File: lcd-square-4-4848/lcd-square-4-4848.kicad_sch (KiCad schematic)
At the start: 43 parts, among them J1 SWD, J2 Conn_01x40_MountingPin, J3 Micro_SD_Card_Det1, SW1 BOOT0, SW2 RST, U1 siplex-som-s16, U2 TPS61169

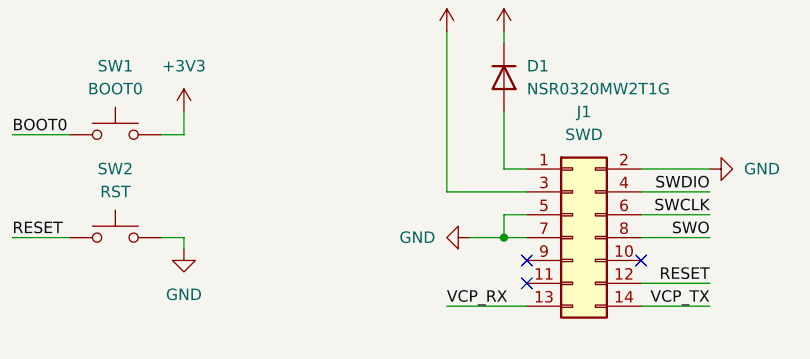
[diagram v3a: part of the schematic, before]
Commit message: LCD 5 inch, Finished SD card, Touch, Buzzer etc, LCD Bar 3.4, Adding resistor on st-link, not finished yet
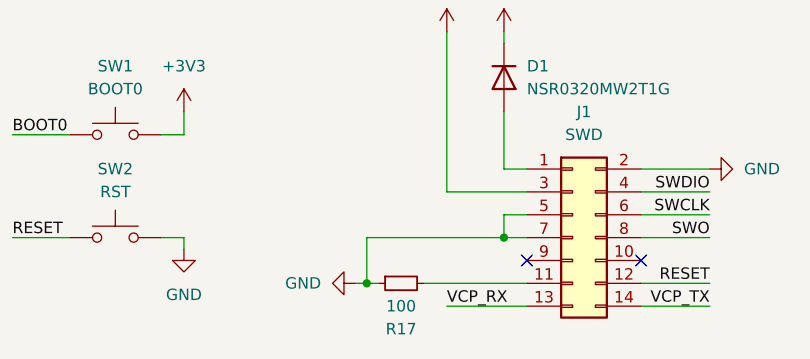
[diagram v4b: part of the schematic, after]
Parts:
- added R17: 100, Resistor_SMD:R_0402_1005Metric, symbol Device:R_Small
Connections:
- net GND: now also R17.1
- net at J1.11 (Pin_11): now also R17.2
- no-connect marks 5 -> 4
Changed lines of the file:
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@@
 	)
 	(junction
+		(at 129.54 189.23)
+		(diameter 0)
+		(color 0 0 0 0)
+	)
+	(junction
 		(at 185.42 66.04)
 		(diameter 0)
@@
 	)
 	(no_connect
-		(at 147.32 189.23)
-	)
-	(no_connect
 		(at 251.46 52.07)
 	)
@@
 	(wire
 		(pts
+			(xy 135.89 189.23) (xy 147.32 189.23)
+		)
+		(stroke
+			(width 0)
+			(type default)
+		)
+	)
+	(wire
+		(pts
 			(xy 24.13 69.85) (xy 36.83 69.85)
 		)
@@
 	(wire
 		(pts
-			(xy 140.97 184.15) (xy 144.78 184.15)
-		)
-		(stroke
-			(width 0)
-			(type default)
-		)
-	)
-	(wire
-		(pts
 			(xy 72.39 52.07) (xy 64.77 52.07)
 		)
@@
 	(wire
 		(pts
+			(xy 129.54 189.23) (xy 130.81 189.23)
+		)
+		(stroke
+			(width 0)
+			(type default)
+		)
+	)
+	(wire
+		(pts
 			(xy 24.13 49.53) (xy 36.83 49.53)
 		)
@@
 	(wire
 		(pts
+			(xy 129.54 184.15) (xy 129.54 189.23)
+		)
+		(stroke
+			(width 0)
+			(type default)
+		)
+	)
+	(wire
+		(pts
 			(xy 24.13 95.25) (xy 36.83 95.25)
 		)
@@
 	(wire
 		(pts
+			(xy 128.27 189.23) (xy 129.54 189.23)
+		)
+		(stroke
+			(width 0)
+			(type default)
+		)
+	)
+	(wire
+		(pts
 			(xy 64.77 39.37) (xy 72.39 39.37)
 		)
@@
 	(wire
 		(pts
+			(xy 129.54 184.15) (xy 144.78 184.15)
+		)
+		(stroke
+			(width 0)
+			(type default)
+		)
+	)
+	(wire
+		(pts
 			(xy 185.42 76.2) (xy 185.42 74.93)
 		)
@@
 	)
 	(symbol
+		(lib_id "power:GND")
+		(at 128.27 189.23 270)
+		(unit 1)
+		(exclude_from_sim no)
+		(in_bom yes)
+		(on_board yes)
+		(dnp no)
+		(fields_autoplaced yes)
+		(property "Reference" "#PWR07"
+			(at 121.92 189.23 0)
+			(effects
+				(font
+					(size 1.27 1.27)
+				)
+				(hide yes)
+			)
+		)
+		(property "Value" "GND"
+			(at 124.46 189.2299 90)
+			(effects
+				(font
+					(size 1.27 1.27)
+				)
+				(justify right)
+			)
+		)
+		(property "Footprint" ""
+			(at 128.27 189.23 0)
+			(effects
+				(font
+					(size 1.27 1.27)
+				)
+				(hide yes)
+			)
+		)
+		(property "Datasheet" ""
+			(at 128.27 189.23 0)
+			(effects
+				(font
+					(size 1.27 1.27)
+				)
+				(hide yes)
+			)
+		)
+		(property "Description" "Power symbol creates a global label with name \"GND\" , ground"
+			(at 128.27 189.23 0)
+			(effects
+				(font
+					(size 1.27 1.27)
+				)
+				(hide yes)
+			)
+		)
+		(pin "1"
+		)
+		(instances
+			(project "lcd-square-4-4848"
+				(path "/a9fe5be7-3a80-455e-a721-d53819db4a52"
+					(reference "#PWR07")
+					(unit 1)
+				)
+			)
+		)
+	)
+	(symbol
 		(lib_id "Device:R_Pack04")
 		(at 95.25 64.77 90)
@@
 	(symbol
 		(lib_id "Device:R_Small")
-		(at 214.63 119.38 0)
-		(mirror y)
+		(at 133.35 189.23 90)
+		(mirror x)
 		(unit 1)
 		(exclude_from_sim no)
@@
 		(on_board yes)
 		(dnp no)
-		(property "Reference" "R5"
-			(at 212.09 118.1099 0)
+		(property "Reference" "R17"
+			(at 133.35 194.31 90)
 			(effects
 				(font
 					(size 1.27 1.27)
 				)
-				(justify left)
 			)
 		)
-		(property "Value" "2K2"
-			(at 212.09 120.6499 0)
+		(property "Value" "100"
+			(at 133.35 191.77 90)
 			(effects
 				(font
 					(size 1.27 1.27)
 				)
-				(justify left)
 			)
 		)
 		(property "Footprint" "Resistor_SMD:R_0402_1005Metric"
-			(at 214.63 119.38 0)
+			(at 133.35 189.23 0)
 			(effects
 				(font
@@
 		)
 		(property "Datasheet" "~"
-			(at 214.63 119.38 0)
+			(at 133.35 189.23 0)
 			(effects
 				(font
@@
 		)
 		(property "Description" "Resistor, small symbol"
-			(at 214.63 119.38 0)
+			(at 133.35 189.23 0)
 			(effects
 				(font
@@
 			)
 		)
-		(pin "2"
-		)
 		(pin "1"
 		)
+		(pin "2"
+		)
 		(instances
 			(project "lcd-square-4-4848"
 				(path "/a9fe5be7-3a80-455e-a721-d53819db4a52"
-					(reference "R5")
+					(reference "R17")
 					(unit 1)
 				)
@@
 	)
 	(symbol
-		(lib_id "power:GND")
-		(at 140.97 184.15 270)
+		(lib_id "Device:R_Small")
+		(at 214.63 119.38 0)
+		(mirror y)
 		(unit 1)
 		(exclude_from_sim no)
@@
 		(on_board yes)
 		(dnp no)
-		(fields_autoplaced yes)
-		(property "Reference" "#PWR010"
-			(at 134.62 184.15 0)
+		(property "Reference" "R5"
+			(at 212.09 118.1099 0)
 			(effects
 				(font
 					(size 1.27 1.27)
 				)
-				(hide yes)
+				(justify left)
 			)
 		)
-		(property "Value" "GND"
-			(at 137.16 184.1499 90)
+		(property "Value" "2K2"
+			(at 212.09 120.6499 0)
 			(effects
 				(font
 					(size 1.27 1.27)
 				)
-				(justify right)
+				(justify left)
 			)
 		)
-		(property "Footprint" ""
-			(at 140.97 184.15 0)
+		(property "Footprint" "Resistor_SMD:R_0402_1005Metric"
+			(at 214.63 119.38 0)
 			(effects
 				(font
@@
 			)
 		)
-		(property "Datasheet" ""
-			(at 140.97 184.15 0)
+		(property "Datasheet" "~"
+			(at 214.63 119.38 0)
 			(effects
 				(font
@@
 			)
 		)
-		(property "Description" "Power symbol creates a global label with name \"GND\" , ground"
-			(at 140.97 184.15 0)
+		(property "Description" "Resistor, small symbol"
+			(at 214.63 119.38 0)
 			(effects
 				(font
@@
 			)
 		)
+		(pin "2"
+		)
 		(pin "1"
 		)
@@
 			(project "lcd-square-4-4848"
 				(path "/a9fe5be7-3a80-455e-a721-d53819db4a52"
-					(reference "#PWR010")
+					(reference "R5")
 					(unit 1)
 				)

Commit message: LCD 5inch, finished tracks, LCD square, Adding MAX98357A
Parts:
- removed U1: siplex-som-s16, siplex:siplex-som-s16, symbol siplex-som:siplex-som-s16
- added C11: 10u, Capacitor_SMD:C_0805_2012Metric, symbol Device:C
- added J5: Conn_01x02_MountingPin, Connector_Hirose:Hirose_DF13C_CL535-0402-2-51_1x02-1MP_P1.25mm_Vertical, symbol Connector_Generic_MountingPin:Conn_01x02_MountingPin
- added R18: 1M, Resistor_SMD:R_0402_1005Metric, symbol Device:R_Small
- added R19: 100K, Resistor_SMD:R_0402_1005Metric, symbol Device:R_Small
- added U1: MAX98357A, Package_DFN_QFN:TQFN-16-1EP_3x3mm_P0.5mm_EP1.23x1.23mm, symbol Audio:MAX98357A
- added U3: siplex-som-s16, siplex:siplex-som-s16, symbol siplex-som:siplex-som-s16
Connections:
- net +3V3: now also U3.42 (3V3_OUT)
- net B0: now also U3.70 (B0)
- net B1: now also U3.71 (B1)
- net B2: now also U3.72 (B2)
- net B3: now also U3.73 (B3)
- net B4: now also U3.74 (B4)
- net B5: now also U3.75 (B5)
- net B6: now also U3.76 (B6)
- net B7: now also U3.77 (B7)
- net BOOT0: now also U3.84 (BOOT0)
- net CLK: now also U3.7 (PC1)
- net CMD: now also U3.9 (PA0)
- net DAT0: now also U3.23 (PB14)
- net DAT1: now also U3.24 (PB15)
- net DAT2: now also U3.39 (PG11)
- net DAT3: now also U3.40 (PB4)
- net G0: now also U3.62 (G0)
- net G1: now also U3.63 (G1)
- net G2: now also U3.64 (G2)
- net G3: now also U3.65 (G3)
- net G4: now also U3.66 (G4)
- net G5: now also U3.67 (G5)
- net G6: now also U3.68 (G6)
- net G7: now also U3.69 (G7)
- net GND: now also C11.2, J5.MP (MountPin), R19.2, U1.11 (GND), U1.15 (GND), U1.17 (PAD), U1.3 (GND), U3.43 (GND), U3.44 (GND), U3.47 (GND), U3.5 (GND), U3.50 (GND), U3.53 (GND), U3.78 (GND), U3.80 (GND), U3.87 (GND)
- net LCD_BLK: now also U3.16 (PB0)
- net LCD_RST: now also U3.14 (PA6)
- net LCD_SPI_CLK: now also U3.15 (PA5)
- net LCD_SPI_CS: now also U3.12 (PA3)
- net LCD_SPI_DAT: now also U3.13 (PA7)
- net LCD_TP_INT: now also U3.1 (PB7)
- net LCD_TP_RST: now also U3.4 (PH4)
- net LCD_TP_SCL: now also U3.2 (PB8)
- net LCD_TP_SDA: now also U3.3 (PB9)
- net LED0: now also U3.22 (PB11)
- net LED1: now also U3.21 (PB13)
- net R0: now also U3.54 (R0)
- net R1: now also U3.55 (R1)
- net R2: now also U3.56 (R2)
- net R3: now also U3.57 (R3)
- net R4: now also U3.58 (R4)
- net R5: now also U3.59 (R5)
- net R6: now also U3.60 (R6)
- net R7: now also U3.61 (R7)
- net RESET: now also U3.85 (RESET)
- net SD_DET: now also U3.25 (PH7)
- net SWCLK: now also U3.46 (SWCLK)
- net SWDIO: now also U3.45 (SWDIO)
- net SWO: now also U3.52 (SWO)
- net USB_DN: now also U3.48 (USB_DN)
- net USB_DP: now also U3.49 (USB_DP)
- net USB_VBUS_DET: now also U3.51 (USB_VBUS_DET)
- net VBAT: now also U3.86 (VBAT)
- net VBUS: now also C11.1, U1.7 (VDD), U1.8 (VDD), U3.41 (VIN)
- net at RN4.5 (R4.2): now also U3.79 (LCD_CLK)
- net at RN4.8 (R1.2): now also U3.83 (LCD_DE)
- net at RN4.7 (R2.2): now also U3.82 (LCD_VSYNC)
- net at RN4.6 (R3.2): now also U3.81 (LCD_HSYNC)
- new net: J5.1 (Pin_1), U1.9 (OUTP)
- new net: J5.2 (Pin_2), U1.10 (OUTN)
- new net: R18.2, U1.4 (~{SD_MODE})
- new net: R19.1, U1.2 (GAIN_SLOT)
- new net I2S_SCLK: U1.16 (BCLK)
- new net I2S_SDO: U1.1 (DIN)
- new net I2S_WS: U1.14 (LRCLK)
- new net ~{SD_MODE}: R18.1

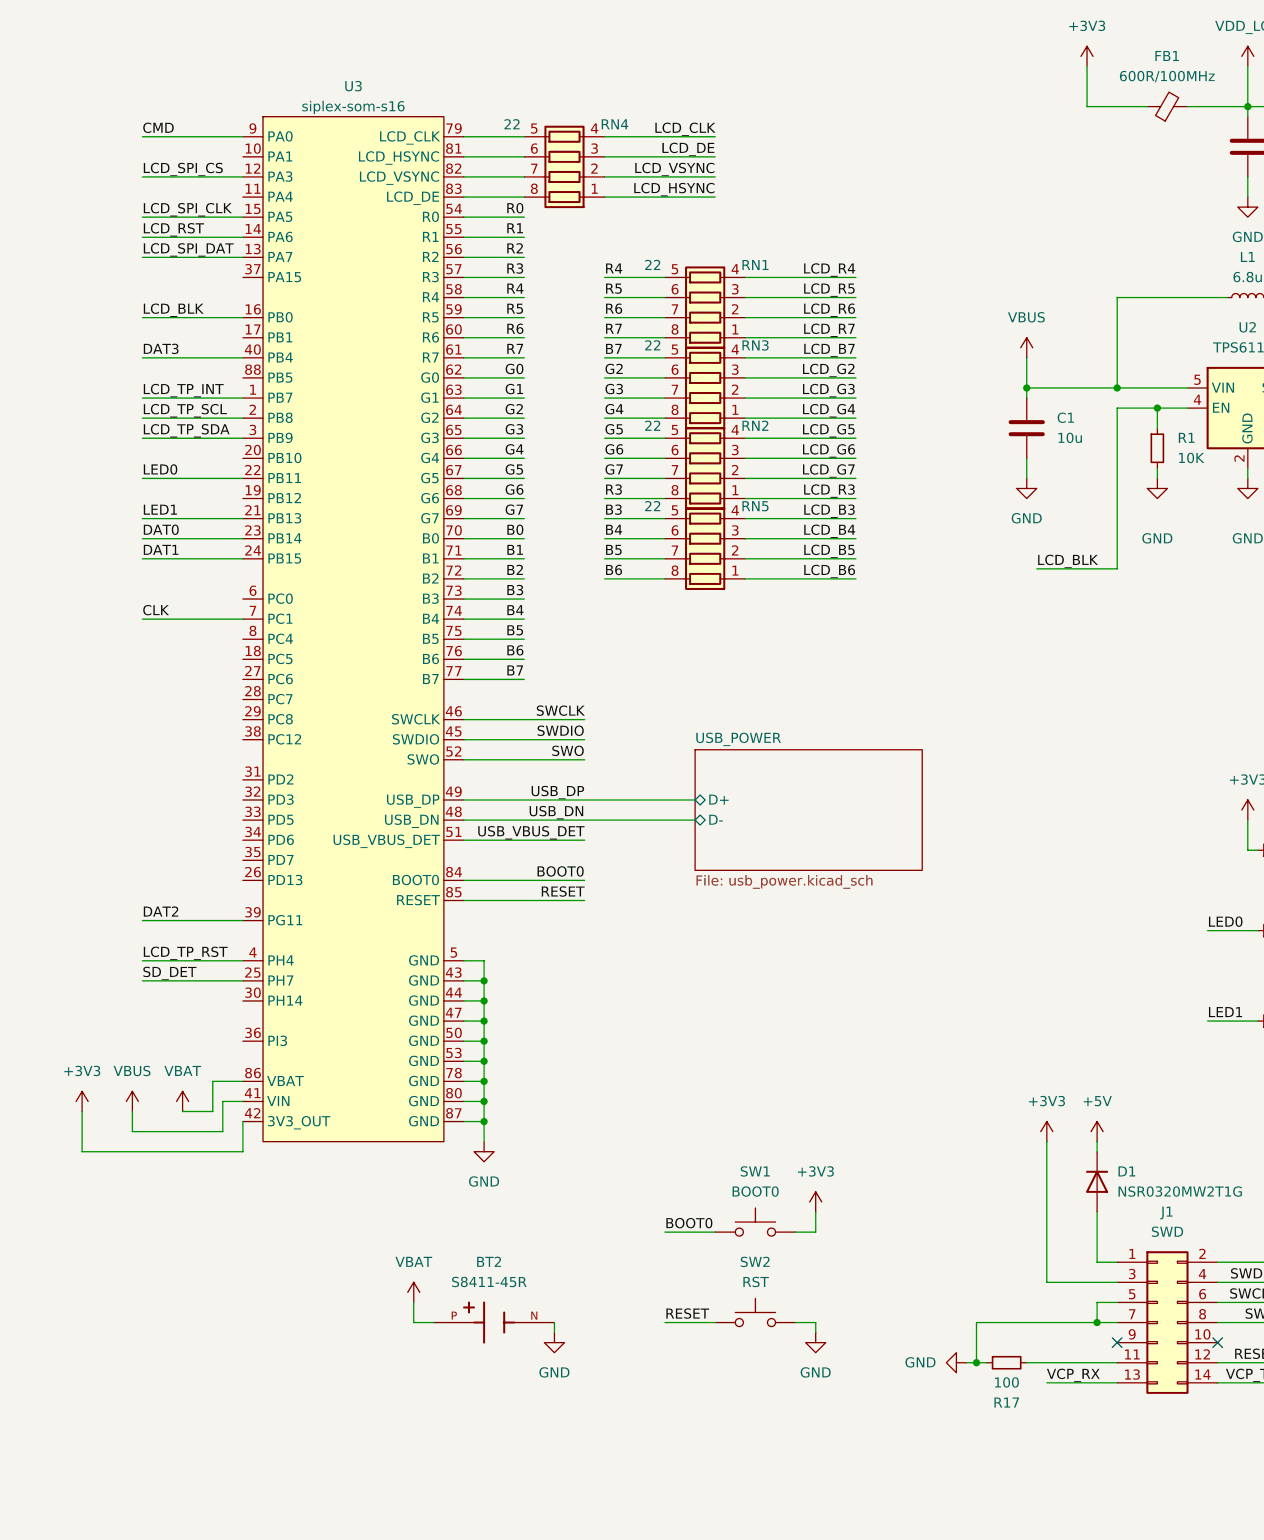
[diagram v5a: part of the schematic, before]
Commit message: Add LCD standard 7inch
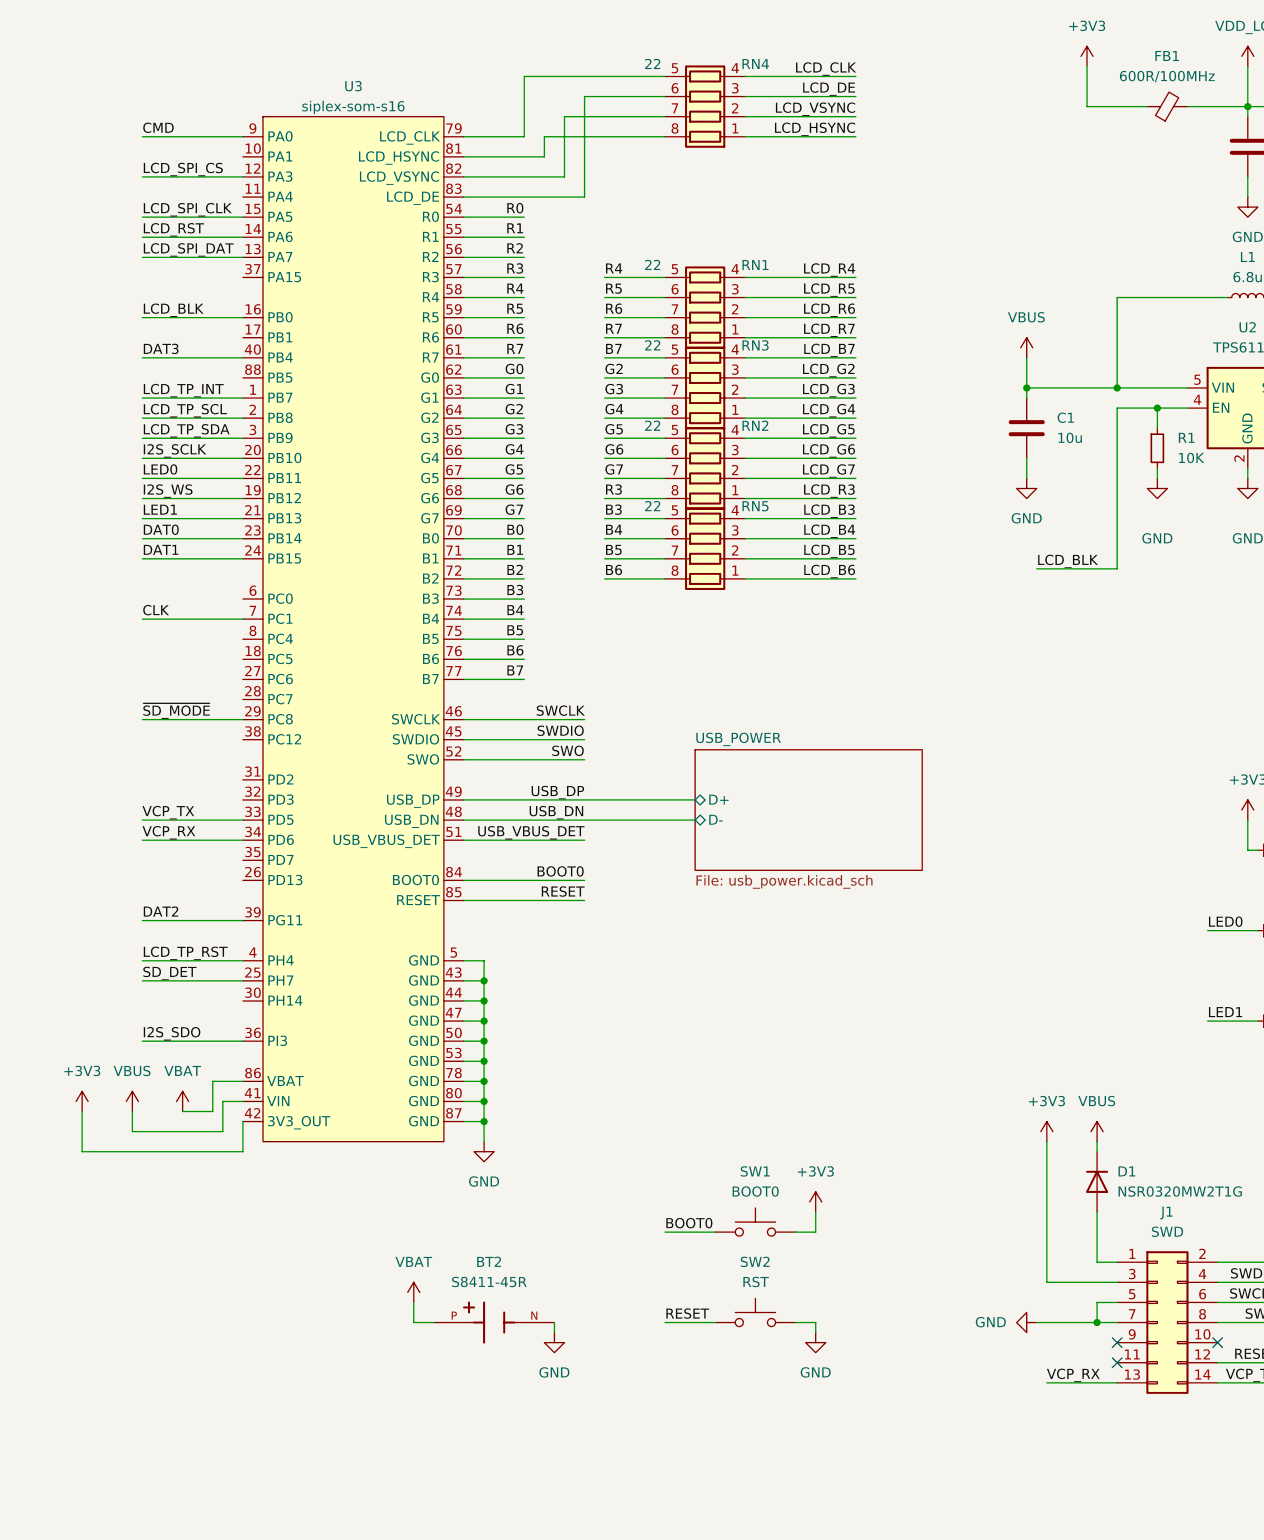
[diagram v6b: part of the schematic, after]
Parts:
- removed R17: 100, Resistor_SMD:R_0402_1005Metric, symbol Device:R_Small
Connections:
- net +5V is gone; now on net VBUS: D1.1 (K)
- net I2S_SCLK: now also U3.20 (PB10)
- net I2S_SDO: now also U3.36 (PI3)
- net I2S_WS: now also U3.19 (PB12)
- net VCP_RX: now also U3.34 (PD6)
- net VCP_TX: now also U3.33 (PD5)
- net ~{SD_MODE}: now also U3.29 (PC8)
- net at U3.81 (LCD_HSYNC): now also RN4.8 (R1.2); no longer RN4.6 (R3.2)
- net at U3.83 (LCD_DE): now also RN4.6 (R3.2); no longer RN4.8 (R1.2)
- no-connect marks 4 -> 5
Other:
- moved on the sheet: RN4

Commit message: Slight changes
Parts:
- BT2: JLCPCB Part # (none) -> C70381
- C1: footprint Capacitor_SMD:C_0603_1608Metric -> Capacitor_SMD:C_0805_2012Metric; JLCPCB Part # (none) -> C15850
- C10, C2, C3: JLCPCB Part # (none) -> C15849
- C11, C5: JLCPCB Part # (none) -> C15850
- C12, C4: JLCPCB Part # (none) -> C307331
- C6, C7: footprint Capacitor_SMD:C_0603_1608Metric -> Capacitor_SMD:C_0402_1005Metric; JLCPCB Part # (none) -> C307331
- D1: JLCPCB Part # (none) -> C48192
- D2: JLCPCB Part # (none) -> C7420330
- D3, D4: value LED -> RED; JLCPCB Part # (none) -> C84256
- D5: value LED -> GREEN; JLCPCB Part # (none) -> C2297
- FB1: JLCPCB Part # (none) -> C1017
- J1: JLCPCB Part # (none) -> C5160763C5160763
- J2: JLCPCB Part # (none) -> C225713
- J3: JLCPCB Part # (none) -> C266621
- J5: JLCPCB Part # (none) -> C7419891
- L1: value 6.8u -> 4.7u; JLCPCB Part # (none) -> C57269
- R1, R12, R13, R14, R15, R4, R7, R8: JLCPCB Part # (none) -> C25744
- R11, R16, R3: JLCPCB Part # (none) -> C4109
- R18: JLCPCB Part # (none) -> C26083
- R19: JLCPCB Part # (none) -> C25741
- R2: footprint Resistor_SMD:R_0402_1005Metric -> Resistor_SMD:R_0603_1608Metric; JLCPCB Part # (none) -> C228038
- R5, R6: JLCPCB Part # (none) -> C25879
- RN1, RN2, RN3, RN4, RN5: value 22 -> 100; JLCPCB Part # (none) -> C48442
- SW1, SW2: JLCPCB Part # (none) -> C127488
- U1: JLCPCB Part # (none) -> C910544
- U2: JLCPCB Part # (none) -> C71045
- U3: now left out of the parts list
